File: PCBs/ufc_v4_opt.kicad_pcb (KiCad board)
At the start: 2 copper layers, 42.9 x 15.9 mm, 71 parts, among them J1 Conn_01x06_Male, J2 Conn_01x06_Male, J3 Conn_01x06_Male, J4 Conn_01x06_Male

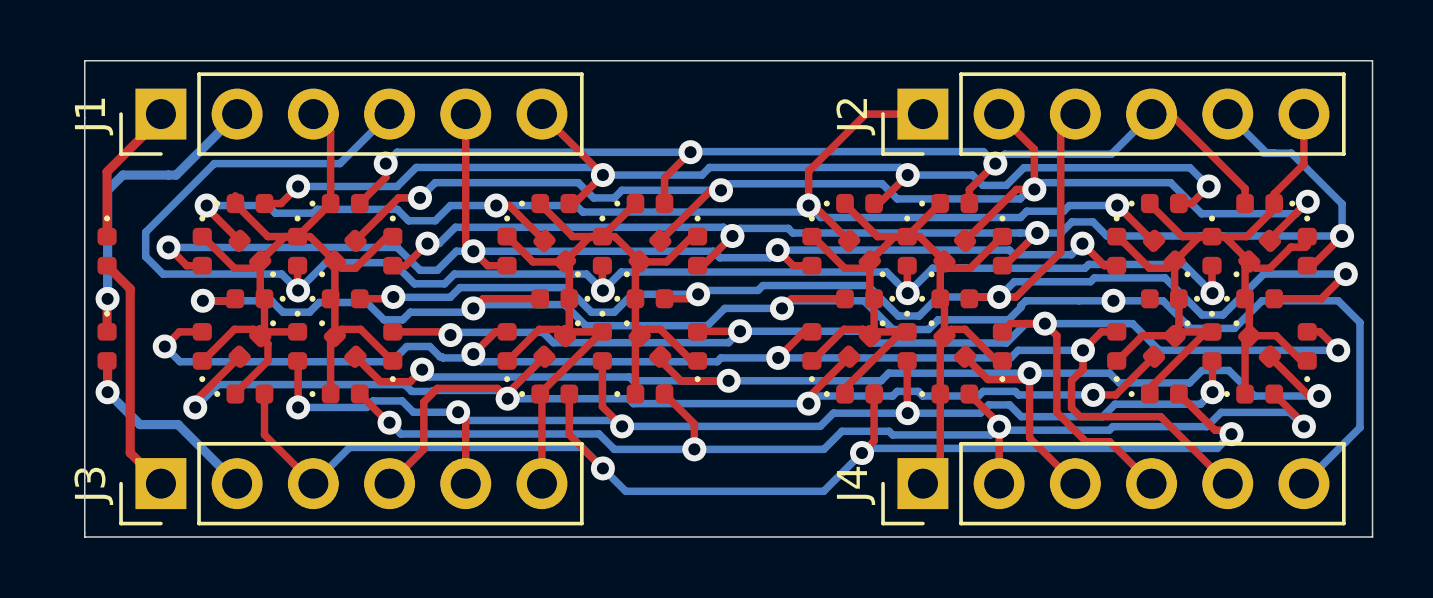
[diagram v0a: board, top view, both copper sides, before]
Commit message: Removed comm displays from PCB
Since they will be connected with wires anyways it didn't make sense to keep them on.
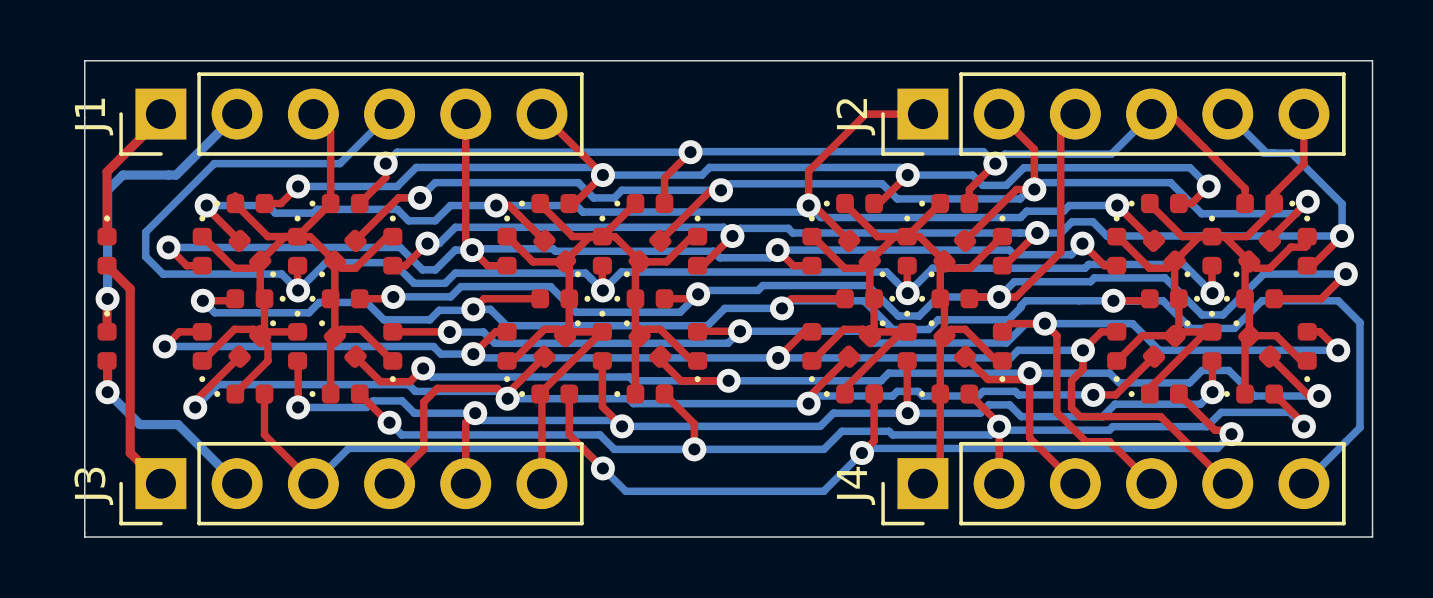
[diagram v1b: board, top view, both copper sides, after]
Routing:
- net /SEGF: track 54.0 -> 55.1 mm
- net /SEGDP: track 45.6 -> 45.0 mm
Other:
- board text added: "SEGH"
- board text added: "SEGJ"
- board text added: "SEGK"
- board text added: "SEGL"
- board text added: "SEGM"
- board text added: "SEGN"
- board text added: "SEGP"
- board text added: "SEGQ"
- board text removed: "DIG4"
- board text removed: "DIG5"
- board text removed: "DIG6"
- board text removed: "DIG7"
